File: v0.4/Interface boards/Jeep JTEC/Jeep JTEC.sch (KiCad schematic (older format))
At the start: 4 parts

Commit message: Add pins for extension hardware
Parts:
- added A?: Arduino_Nano_v3.x, Module:Arduino_Nano, symbol MCU_Module:Arduino_Nano_v3.x
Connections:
- net labels added: AC_CLUTCH_OUT, AC_PRESSURE_SWITCH, AC_SELECT, ASD_12V_IN, ASD_COIL_OUT, BATTERY_TEMP, BRAKE_LAMP_SWITCH, CCD+, CCD-, CRUISE_PWR_OUT, CRUISE_VACUUM, CRUISE_VENT, EVAP_SOLENOID, FUEL_LEVEL, GENERATOR_12v+, GENERATOR_GND, LEAK_DETECT_SOLENOID, LEAK_DETECT_SWITCH_SENSE, OIL_PRESSURE_IN, RAD_FAN_REQUEST, SPEED_CONTROL_SWITCH
- net labels removed: ASD_OUT, OIL-PRESSURE-IN
- wire segments 86 -> 110
- no-connect marks 36 -> 38
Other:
- note added: "Brake lamp switch sense\nis normally grounded"
- note added: "Italic labels indicate signals that are not used\non this breakout board"
- note added: "Reference 1: https://www.cherokeeforum.com/f67/guide-megasquirt-4-0-a-254321/\nReference 2: https://mopar1973man.com/cummins/articles.html/24-valve-2nd-generation_50/51_engine/electrical/ccd-chrysler-collision-detection-data-bus-r329/\nReference 3: https://azxiana.io/2017/04/09/creating-a-chrysler-pcmecu-simulator/"
- note removed: "Reference 1: https://www.cherokeeforum.com/f67/guide-megasquirt-4-0-a-254321/"
- moved on the sheet: C3

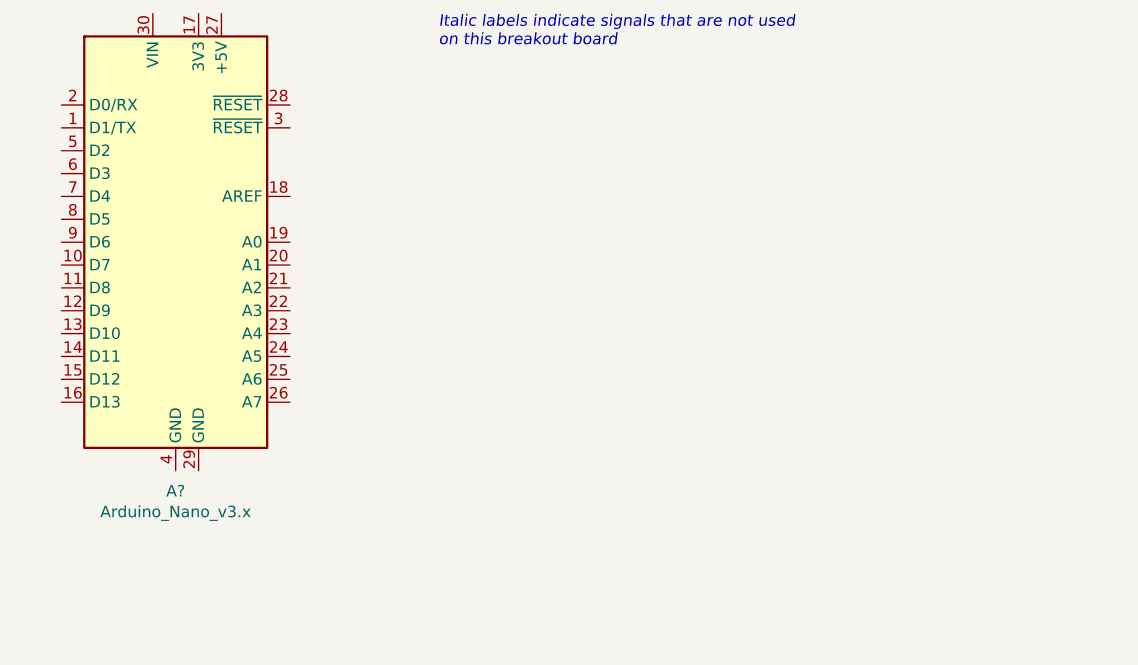
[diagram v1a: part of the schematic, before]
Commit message: Start building CCD output stage
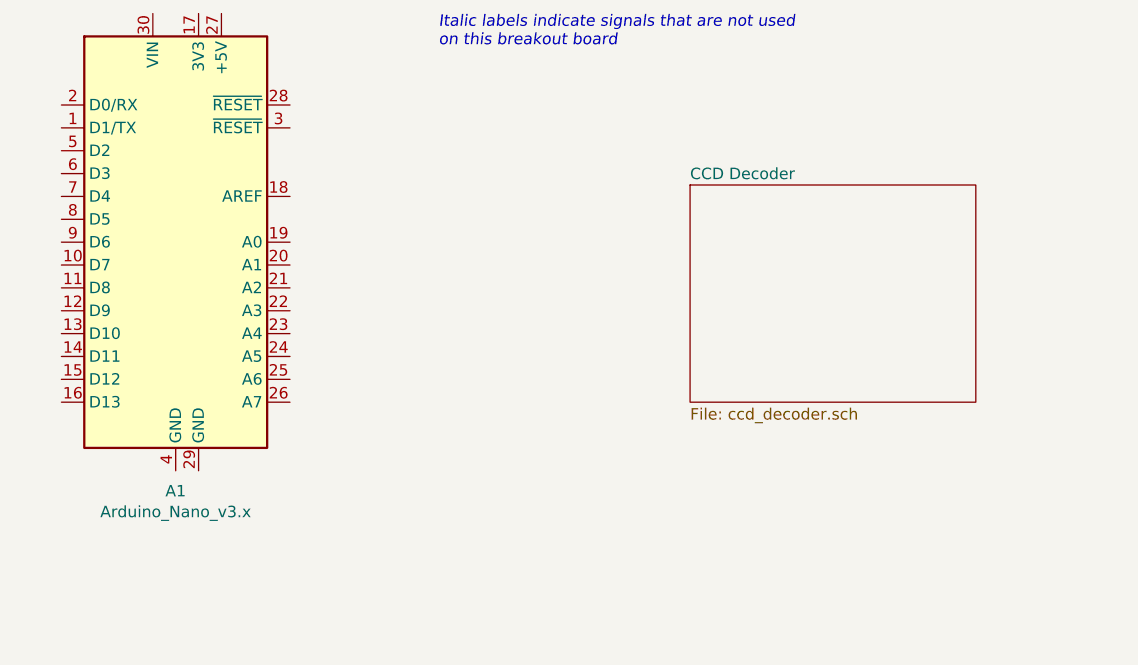
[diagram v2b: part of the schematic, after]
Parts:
- gave numbers to parts that had none: 2
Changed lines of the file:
@@
 $Descr A4 11693 8268
 encoding utf-8
-Sheet 1 1
+Sheet 1 2
 Title "Jeep JTEC Breakout"
 Date "2021-09-28"
@@
 $EndDescr
 $Comp
-L power:GNDA #PWR?
+L power:GNDA #PWR01
 U 1 1 5CF08983
 P 1050 2100
-F 0 "#PWR?" H 1050 1850 50  0001 C CNN
+F 0 "#PWR01" H 1050 1850 50  0001 C CNN
 F 1 "GNDA" V 1055 1972 50  0000 R CNN
 F 2 "" H 1050 2100 50  0001 C CNN
@@
 IAT_Sensor
 $Comp
-L power:VDDA #PWR?
+L power:VDDA #PWR02
 U 1 1 5CF9256D
 P 1350 2450
-F 0 "#PWR?" H 1350 2300 50  0001 C CNN
+F 0 "#PWR02" H 1350 2300 50  0001 C CNN
 F 1 "VDDA" V 1368 2578 50  0000 L CNN
 F 2 "" H 1350 2450 50  0001 C CNN
@@
 CAM-IN
 $Comp
-L Connector_Generic:Conn_02x20_Counter_Clockwise J?
+L Connector_Generic:Conn_02x20_Counter_Clockwise J1
 U 1 1 5CF56B69
 P 1700 2150
-F 0 "J?" H 1750 3267 50  0000 C CNN
+F 0 "J1" H 1750 3267 50  0000 C CNN
 F 1 "Conn_02x20_Counter_Clockwise" H 1750 3176 50  0000 C CNN
 F 2 "Connector_IDC:IDC-Header_2x20_P2.54mm_Vertical" H 1700 2150 50  0001 C CNN
@@
 	1400 1850 1500 1850
 $Comp
-L power:GNDA #PWR?
+L power:GNDA #PWR03
 U 1 1 5CF6E3B5
 P 1400 2350
-F 0 "#PWR?" H 1400 2100 50  0001 C CNN
+F 0 "#PWR03" H 1400 2100 50  0001 C CNN
 F 1 "GNDA" V 1405 2222 50  0000 R CNN
 F 2 "" H 1400 2350 50  0001 C CNN
@@
 TPS_Sensor
 $Comp
-L power:GNDA #PWR?
+L power:GNDA #PWR06
 U 1 1 5CF523DE
 P 2100 2950
-F 0 "#PWR?" H 2100 2700 50  0001 C CNN
+F 0 "#PWR06" H 2100 2700 50  0001 C CNN
 F 1 "GNDA" V 2105 2822 50  0000 R CNN
 F 2 "" H 2100 2950 50  0001 C CNN
@@
 VR1-
 $Comp
-L power:VDDA #PWR?
+L power:VDDA #PWR05
 U 1 1 5CF58939
 P 2100 2450
-F 0 "#PWR?" H 2100 2300 50  0001 C CNN
+F 0 "#PWR05" H 2100 2300 50  0001 C CNN
 F 1 "VDDA" V 2118 2578 50  0000 L CNN
 F 2 "" H 2100 2450 50  0001 C CNN
@@
 	7400 2500 7500 2500
 $Comp
-L power:GNDA #PWR?
+L power:GNDA #PWR07
 U 1 1 615AA12C
 P 4900 1300
-F 0 "#PWR?" H 4900 1050 50  0001 C CNN
+F 0 "#PWR07" H 4900 1050 50  0001 C CNN
 F 1 "GNDA" V 4905 1172 50  0000 R CNN
 F 2 "" H 4900 1300 50  0001 C CNN
@@
 	4900 3200 5000 3200
 $Comp
-L power:VDDA #PWR?
+L power:VDDA #PWR08
 U 1 1 615BDD6F
 P 4900 2600
-F 0 "#PWR?" H 4900 2450 50  0001 C CNN
+F 0 "#PWR08" H 4900 2450 50  0001 C CNN
 F 1 "VDDA" V 4918 2728 50  0000 L CNN
 F 2 "" H 4900 2600 50  0001 C CNN
@@
 	4900 3600 5000 3600
 $Comp
-L power:VDDA #PWR?
+L power:VDDA #PWR011
 U 1 1 615C91A8
 P 7400 4000
-F 0 "#PWR?" H 7400 3850 50  0001 C CNN
+F 0 "#PWR011" H 7400 3850 50  0001 C CNN
 F 1 "VDDA" V 7418 4128 50  0000 L CNN
 F 2 "" H 7400 4000 50  0001 C CNN
@@
 	4900 1100 5000 1100
 $Comp
-L power:GND #PWR?
+L power:GND #PWR09
 U 1 1 616434E1
 P 4900 4000
-F 0 "#PWR?" H 4900 3750 50  0001 C CNN
+F 0 "#PWR09" H 4900 3750 50  0001 C CNN
 F 1 "GND" V 4905 3872 50  0000 R CNN
 F 2 "" H 4900 4000 50  0001 C CNN
@@
 $EndComp
 $Comp
-L power:GND #PWR?
+L power:GND #PWR010
 U 1 1 61643982
 P 4900 4100
-F 0 "#PWR?" H 4900 3850 50  0001 C CNN
+F 0 "#PWR010" H 4900 3850 50  0001 C CNN
 F 1 "GND" V 4905 3972 50  0000 R CNN
 F 2 "" H 4900 4100 50  0001 C CNN
@@
 	4900 4100 5000 4100
 $Comp
-L power:GND #PWR?
+L power:GND #PWR04
 U 1 1 616493D9
 P 1600 4900
-F 0 "#PWR?" H 1600 4650 50  0001 C CNN
+F 0 "#PWR04" H 1600 4650 50  0001 C CNN
 F 1 "GND" V 1605 4772 50  0000 R CNN
 F 2 "" H 1600 4900 50  0001 C CNN
@@
 Italic labels indicate signals that are not used\non this breakout board
 $Comp
-L MCU_Module:Arduino_Nano_v3.x A?
+L MCU_Module:Arduino_Nano_v3.x A1
 U 1 1 6153DDCF
 P 6550 5450
-F 0 "A?" H 6550 4361 50  0000 C CNN
+F 0 "A1" H 6550 4361 50  0000 C CNN
 F 1 "Arduino_Nano_v3.x" H 6550 4270 50  0000 C CNN
 F 2 "Module:Arduino_Nano" H 6550 5450 50  0001 C CIN
@@
 Text HLabel 7400 3200 0    50   Input Italic 0
 OIL_PRESSURE_IN
+$Sheet
+S 8800 5200 1250 950
+U 615FCF77
+F0 "CCD Decoder" 50
+F1 "ccd_decoder.sch" 50
+$EndSheet
 $EndSCHEMATC

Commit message: Draw Jeep igniters and cruise control drivers
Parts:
- added R?: 10k, symbol Device:R_Small
- C1, C2, C3: footprint (none) -> Connector_Automotive:mopar_32pin_pcm
- J1: symbol Connector_Generic:Conn_02x20_Counter_Clockwise -> Connector_Generic:Conn_02x20_Odd_Even
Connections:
- net labels added: CRUISE_VAC_CONTROL, CRUISE_VAC_OUT, CRUISE_VENT_CONTROL, CRUISE_VENT_OUT, IGN-1-DRIVER, IGN-2-DRIVER, IGN-3-DRIVER, PNP_SW
- net labels removed: CRUISE_VACUUM, CRUISE_VENT
- wire segments 110 -> 150
- no-connect marks 38 -> 37
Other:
- note added: "AC clutch grounded = On"
- note added: "AC_SELECT grounded when on"
- note added: "D2 and D3 are INT pins"
- note added: "Pressure switch grounded when ok"
- note added: "Solenoid grounded = On"
- moved on the sheet: A1, C2, C3
